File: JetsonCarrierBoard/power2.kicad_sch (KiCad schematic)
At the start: 19 parts

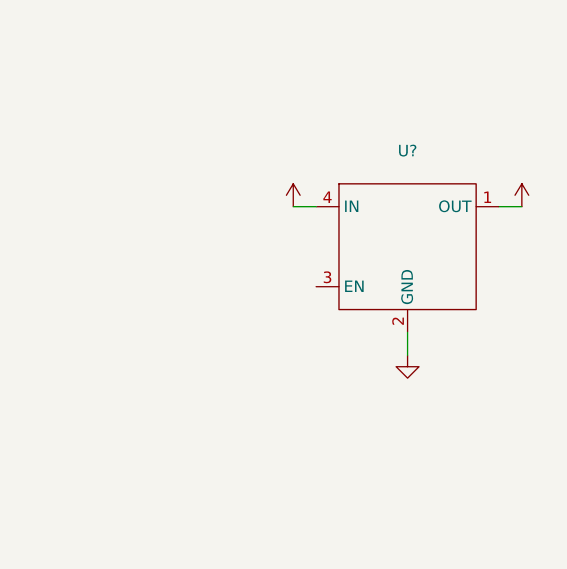
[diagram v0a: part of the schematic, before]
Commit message: Added all USB-C components and started M.2 WiFi
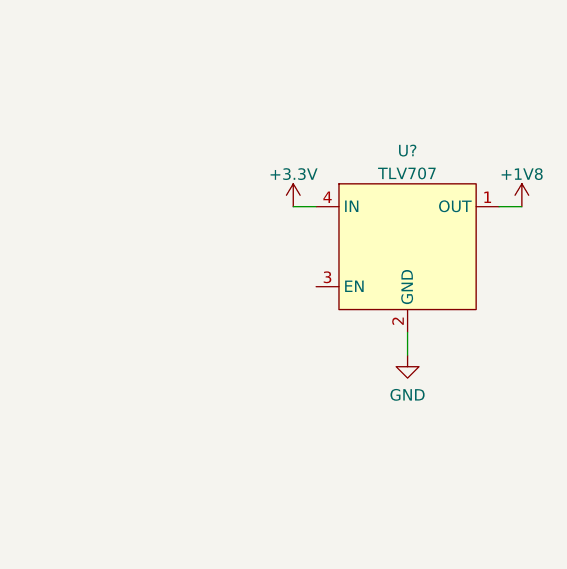
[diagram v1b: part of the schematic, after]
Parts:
- U?: value (none) -> TLV707
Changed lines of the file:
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@@
       (effects (font (size 1.27 1.27)) hide)
     )
-    (property "Value" "" (id 1) (at 218.44 54.8442 0))
+    (property "Value" "+1V8" (id 1) (at 218.44 54.8442 0))
     (property "Footprint" "" (id 2) (at 218.44 58.42 0)
       (effects (font (size 1.27 1.27)) hide)
@@
     (in_bom yes) (on_board yes) (fields_autoplaced)
     (property "Reference" "U?" (id 0) (at 205.74 52.231 0))
-    (property "Value" "" (id 1) (at 205.74 54.7679 0))
+    (property "Value" "TLV707" (id 1) (at 205.74 54.7679 0))
     (property "Footprint" "" (id 2) (at 205.74 54.61 0)
       (effects (font (size 1.27 1.27)) hide)
     )
-    (property "Datasheet" "" (id 3) (at 205.74 54.61 0)
+    (property "Datasheet" "https://www.ti.com/lit/ds/symlink/tlv707.pdf" (id 3) (at 205.74 54.61 0)
       (effects (font (size 1.27 1.27)) hide)
     )
@@
       (effects (font (size 1.27 1.27)) hide)
     )
-    (property "Value" "" (id 1) (at 193.04 54.8442 0))
+    (property "Value" "+3.3V" (id 1) (at 193.04 54.8442 0))
     (property "Footprint" "" (id 2) (at 193.04 58.42 0)
       (effects (font (size 1.27 1.27)) hide)
@@
       (effects (font (size 1.27 1.27)) hide)
     )
-    (property "Datasheet" "" (id 3) (at 76.2 48.26 0)
+    (property "Datasheet" "https://www.vishay.com/docs/75921/sic437.pdf" (id 3) (at 76.2 48.26 0)
       (effects (font (size 1.27 1.27)) hide)
     )
@@
       (effects (font (size 1.27 1.27)) hide)
     )
-    (property "Value" "" (id 1) (at 205.74 79.3734 0))
+    (property "Value" "GND" (id 1) (at 205.74 79.3734 0))
     (property "Footprint" "" (id 2) (at 205.74 74.93 0)
       (effects (font (size 1.27 1.27)) hide)
